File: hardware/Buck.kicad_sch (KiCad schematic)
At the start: 14 parts, among them U901 MT2499A

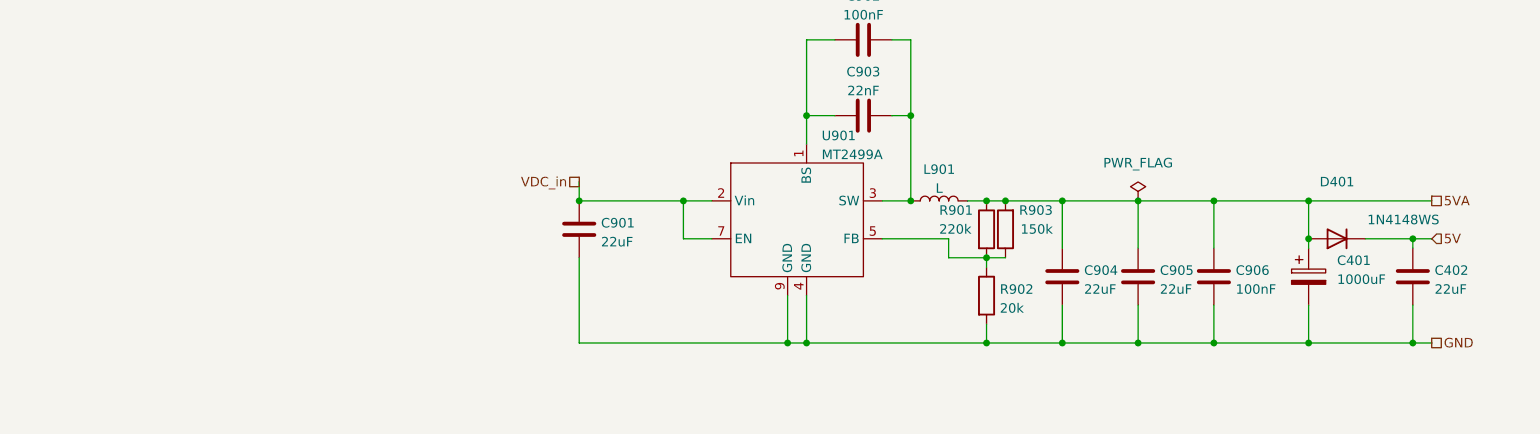
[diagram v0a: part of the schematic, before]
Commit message: update board file, made similar to OS solenoid decoder
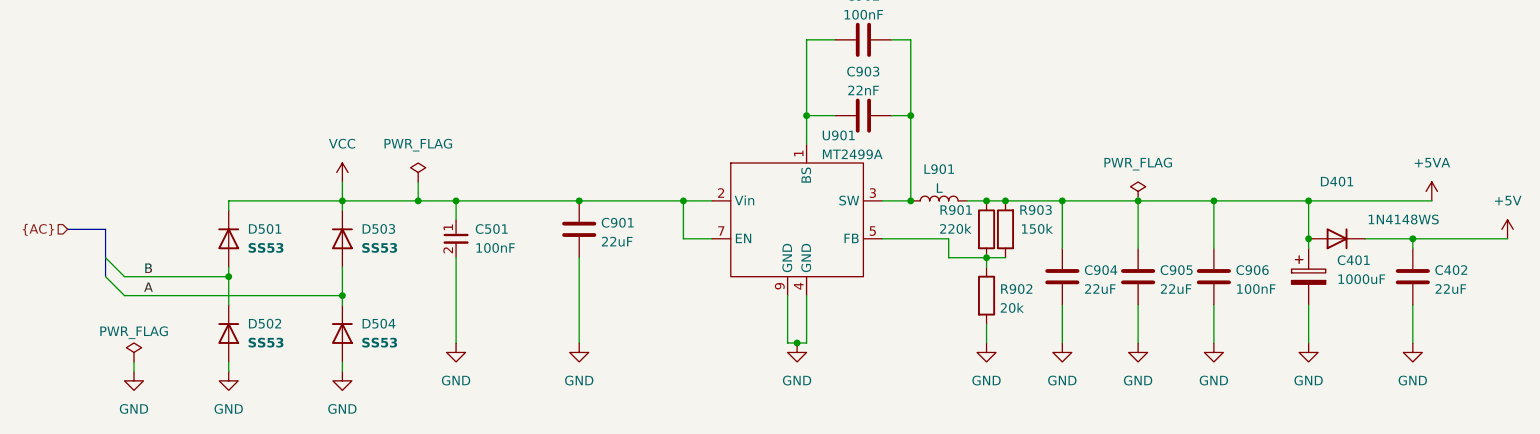
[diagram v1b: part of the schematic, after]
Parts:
- added C501: 100nF, Capacitor_SMD:C_0603_1608Metric, symbol capacitor_miscellaneous:C_0603_100nF
- added D501, D502, D503, D504: SS53, Diode_SMD:D_SMA, symbol custom_kicad_lib_sk:SS53
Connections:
- net GND: now also C501.2, D502.2 (A), D504.2 (A)
- net 5V renamed +5V
- net 5VA renamed +5VA
- net VDC_in renamed VCC
- net VCC: now also C501.1, D501.1 (K), D503.1 (K)
- new net A: D503.2 (A), D504.1 (K)
- new net B: D501.2 (A), D502.1 (K)

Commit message: added manual and picture
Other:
- moved on the sheet: C401, C402, C501, C901, C902, C903, C904, C905, C906, D401, D501, D502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
